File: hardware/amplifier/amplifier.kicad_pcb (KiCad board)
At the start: 2 copper layers, 107.1 x 39.9 mm, 15 parts, among them K101 CONN_3, K102 Out, P101 Sensor, U101 LT1010, U102 INA2128, U103 LT1010

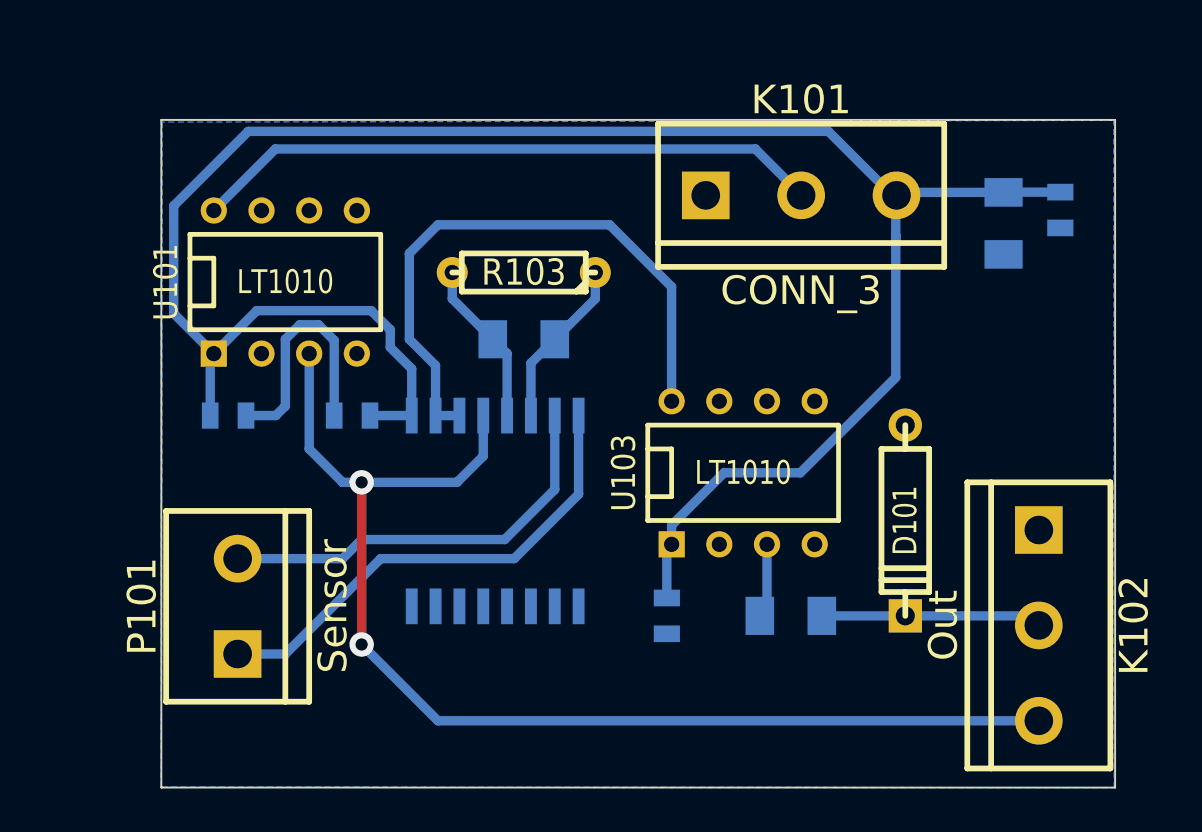
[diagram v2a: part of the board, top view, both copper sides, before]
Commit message: Placing of component designators on silk screen.
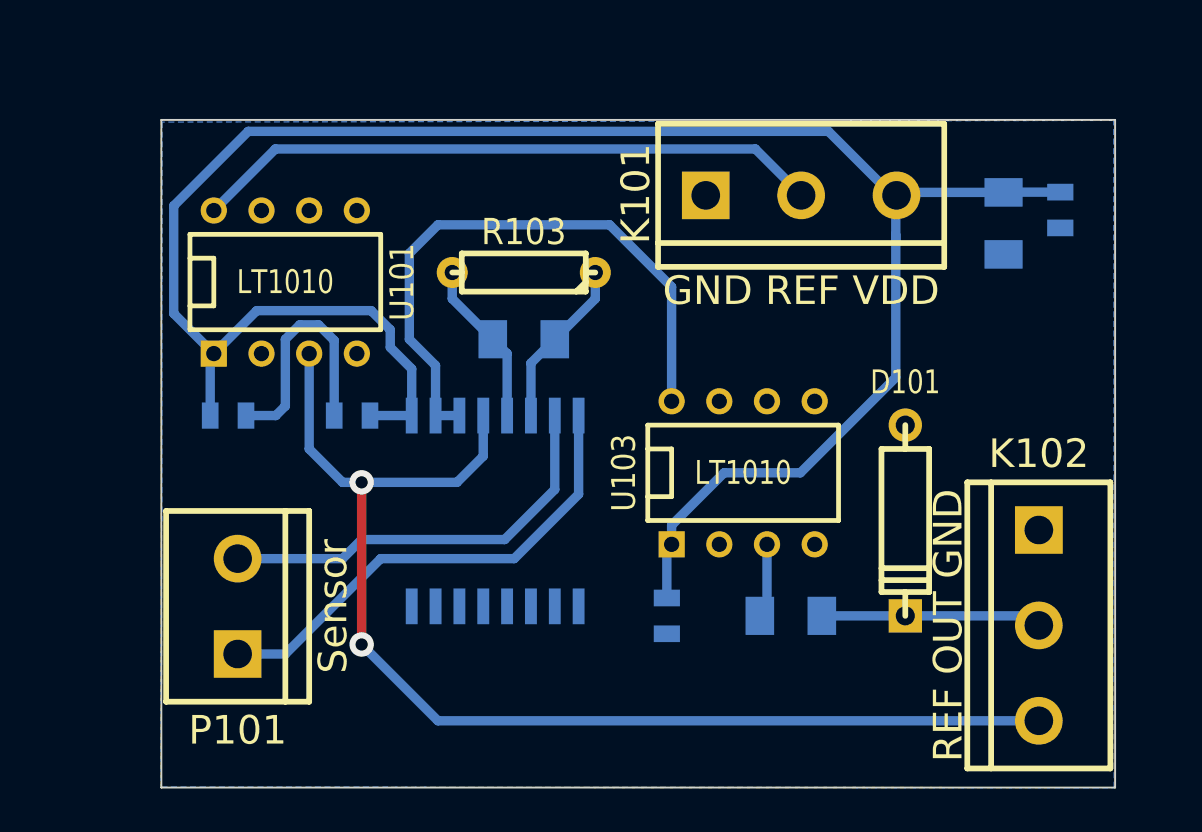
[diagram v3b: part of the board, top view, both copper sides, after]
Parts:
- K101: value CONN_3 -> GND REF VDD
- K102: value Out -> REF OUT GND
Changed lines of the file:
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@@
-(kicad_pcb (version 3) (host pcbnew "(2013-07-07 BZR 4022)-stable")
+(kicad_pcb (version 3) (host pcbnew "(2013-jul-07)-stable")
   (general
     (links 32)
@@
     (at 287.02 138.684 180)
     (attr smd)
-    (fp_text reference U102 (at 0 -1.524 180) (layer B.SilkS)
+    (fp_text reference U102 (at 0 -7.493 180) (layer B.SilkS)
       (effects (font (size 1.143 1.143) (thickness 0.2032)) (justify mirror))
     )
-    (fp_text value INA2128 (at 0.381 1.905 180) (layer B.SilkS) hide
+    (fp_text value INA2128 (at 0 0 180) (layer B.SilkS) hide
       (effects (font (size 1.143 1.143) (thickness 0.2032)) (justify mirror))
     )
@@
     (at 288.544 129.54 180)
     (attr smd)
-    (fp_text reference R102 (at 0 0 180) (layer B.SilkS)
+    (fp_text reference R102 (at 0 1.905 180) (layer B.SilkS)
       (effects (font (size 0.762 0.762) (thickness 0.127)) (justify mirror))
     )
@@
     (at 302.768 144.272 180)
     (attr smd)
-    (fp_text reference R101 (at 0 0 180) (layer B.SilkS)
+    (fp_text reference R101 (at 1.651 -2.159 180) (layer B.SilkS)
       (effects (font (size 0.762 0.762) (thickness 0.127)) (justify mirror))
     )
-    (fp_text value 1K (at 0 0 180) (layer B.SilkS) hide
+    (fp_text value 1K (at -1.905 -2.159 180) (layer B.SilkS) hide
       (effects (font (size 0.762 0.762) (thickness 0.127)) (justify mirror))
     )
@@
     (at 314.0964 123.3678 270)
     (attr smd)
-    (fp_text reference C103 (at 0 0 270) (layer B.SilkS)
+    (fp_text reference C103 (at -3.4798 0.0254 360) (layer B.SilkS)
       (effects (font (size 0.762 0.762) (thickness 0.127)) (justify mirror))
     )
-    (fp_text value 10uF (at 0 0 270) (layer B.SilkS) hide
+    (fp_text value 10uF (at 3.6322 0.0254 360) (layer B.SilkS) hide
       (effects (font (size 0.762 0.762) (thickness 0.127)) (justify mirror))
     )
@@
     (at 317.119 122.6566 270)
     (attr smd)
-    (fp_text reference C102 (at 0 0.3175 270) (layer B.SilkS)
-      (effects (font (size 0.50038 0.50038) (thickness 0.10922)) (justify mirror))
-    )
-    (fp_text value 1uF (at 0 -0.381 270) (layer B.SilkS)
+    (fp_text reference C102 (at -2.2606 0 360) (layer B.SilkS)
+      (effects (font (size 0.50038 0.50038) (thickness 0.10922)) (justify mirror))
+    )
+    (fp_text value 1uF (at 2.3114 0 360) (layer B.SilkS)
       (effects (font (size 0.50038 0.50038) (thickness 0.10922)) (justify mirror))
     )
@@
     (at 272.796 133.604)
     (attr smd)
-    (fp_text reference C105 (at 0 0.3175) (layer B.SilkS)
-      (effects (font (size 0.50038 0.50038) (thickness 0.10922)) (justify mirror))
-    )
-    (fp_text value 0.1uF (at 0 -0.381) (layer B.SilkS)
+    (fp_text reference C105 (at 2.413 0 90) (layer B.SilkS)
+      (effects (font (size 0.50038 0.50038) (thickness 0.10922)) (justify mirror))
+    )
+    (fp_text value 0.1uF (at -2.286 0 90) (layer B.SilkS)
       (effects (font (size 0.50038 0.50038) (thickness 0.10922)) (justify mirror))
     )
@@
     (at 279.4 133.604 180)
     (attr smd)
-    (fp_text reference C104 (at 0 0.3175 180) (layer B.SilkS)
-      (effects (font (size 0.50038 0.50038) (thickness 0.10922)) (justify mirror))
-    )
-    (fp_text value 0.1uF (at 0 -0.381 180) (layer B.SilkS)
+    (fp_text reference C104 (at 0 1.397 180) (layer B.SilkS)
+      (effects (font (size 0.50038 0.50038) (thickness 0.10922)) (justify mirror))
+    )
+    (fp_text value 0.1uF (at 0 -1.524 180) (layer B.SilkS)
       (effects (font (size 0.50038 0.50038) (thickness 0.10922)) (justify mirror))
     )
@@
     (at 296.164 144.272 270)
     (attr smd)
-    (fp_text reference C101 (at 0 0.3175 270) (layer B.SilkS)
-      (effects (font (size 0.50038 0.50038) (thickness 0.10922)) (justify mirror))
-    )
-    (fp_text value 0.1uF (at 0 -0.381 270) (layer B.SilkS)
+    (fp_text reference C101 (at 0 1.651 270) (layer B.SilkS)
+      (effects (font (size 0.50038 0.50038) (thickness 0.10922)) (justify mirror))
+    )
+    (fp_text value 0.1uF (at 0 -1.651 270) (layer B.SilkS)
       (effects (font (size 0.50038 0.50038) (thickness 0.10922)) (justify mirror))
     )
@@
     (tags R)
     (autoplace_cost180 10)
-    (fp_text reference R103 (at 0 0 180) (layer F.SilkS)
+    (fp_text reference R103 (at 0 2.159 180) (layer F.SilkS)
       (effects (font (size 1.397 1.27) (thickness 0.2032)))
     )
@@
     (descr "8 pins DIL package, round pads")
     (tags DIL)
-    (fp_text reference U101 (at -6.35 0 90) (layer F.SilkS)
+    (fp_text reference U101 (at 6.223 0 90) (layer F.SilkS)
       (effects (font (size 1.27 1.143) (thickness 0.2032)))
     )
@@
     (descr "Diode 4 pas")
     (tags "DIODE DEV")
-    (fp_text reference D101 (at 0 0 270) (layer F.SilkS)
+    (fp_text reference D101 (at -7.366 0 360) (layer F.SilkS)
       (effects (font (size 1.27 1.016) (thickness 0.2032)))
     )
-    (fp_text value 1N4732 (at 0 0 270) (layer F.SilkS) hide
+    (fp_text value 1N4732 (at 0 2.159 270) (layer F.SilkS) hide
       (effects (font (size 1.27 1.016) (thickness 0.2032)))
     )
@@
     (descr "Bornier d'alimentation 3 pins")
     (tags DEV)
-    (fp_text reference K102 (at 0 -5.08 270) (layer F.SilkS)
+    (fp_text reference K102 (at -9.144 0 360) (layer F.SilkS)
       (effects (font (size 1.524 1.524) (thickness 0.3048)))
     )
-    (fp_text value Out (at 0 5.08 270) (layer F.SilkS)
+    (fp_text value "REF OUT GND" (at 0 4.826 270) (layer F.SilkS)
       (effects (font (size 1.524 1.524) (thickness 0.3048)))
     )
@@
     (descr "Bornier d'alimentation 3 pins")
     (tags DEV)
-    (fp_text reference K101 (at 0 -5.08) (layer F.SilkS)
+    (fp_text reference K101 (at -8.80364 -0.08128 90) (layer F.SilkS)
       (effects (font (size 1.524 1.524) (thickness 0.3048)))
     )
-    (fp_text value CONN_3 (at 0 5.08) (layer F.SilkS)
+    (fp_text value "GND REF VDD" (at 0 5.08) (layer F.SilkS)
       (effects (font (size 1.524 1.524) (thickness 0.3048)))
     )
@@
     (descr "Bornier d'alimentation 2 pins")
     (tags DEV)
-    (fp_text reference P101 (at 0 -5.08 90) (layer F.SilkS)
+    (fp_text reference P101 (at -6.604 0 180) (layer F.SilkS)
       (effects (font (size 1.524 1.524) (thickness 0.3048)))
     )
